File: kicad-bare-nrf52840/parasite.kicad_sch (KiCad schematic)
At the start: 29 parts, among them Q1 MMBT3906, Q4 Q_Photo_NPN, SW1 B3U-1000P, U1 E73-2G4M08S1C, U2 SHTC3, Y1 32.768kHz

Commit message: feat: capture bare nRF52840 circuit with verified Nordic support networks
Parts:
- removed RST1, SW1: B3U-1000P, SW_B3U-1000P, symbol B3U-1000P:B3U-1000P
- removed U1: E73-2G4M08S1C, snapeda:E73-2G4M08S1C, symbol E73:E73-2G4M08S1C
- added AE1: 2450AT18B0100001E, RF_Antenna:Johanson_2450AT18x100, symbol Device:Antenna_Chip
- added C10, C5, C8, C9: 100n, Capacitor_SMD:C_0402_1005Metric, symbol Device:C_Small
- added C11, C7: 1u, Capacitor_SMD:C_0402_1005Metric, symbol Device:C_Small
- added C12: 47n, Capacitor_SMD:C_0402_1005Metric, symbol Device:C_Small
- added C13: 100p, Capacitor_SMD:C_0402_1005Metric, symbol Device:C_Small
- added C14, C15: 12p, Capacitor_SMD:C_0402_1005Metric, symbol Device:C_Small
- added C16: 820p, Capacitor_SMD:C_0402_1005Metric, symbol Device:C_Small
- added C17: 0.8p, Capacitor_SMD:C_0402_1005Metric, symbol Device:C_Small
- added C18: 0.5p, Capacitor_SMD:C_0402_1005Metric, symbol Device:C_Small
- added C19: 1.2p, Capacitor_SMD:C_0402_1005Metric, symbol Device:C_Small
- added C6: 4.7u, Capacitor_SMD:C_0402_1005Metric, symbol Device:C_Small
- added L1: 10u, Inductor_SMD:L_0603_1608Metric, symbol Device:L
- added L2: 15n, Inductor_SMD:L_0402_1005Metric, symbol Device:L
- added L3: 4.7n, Inductor_SMD:L_0402_1005Metric, symbol Device:L
- added L4: 2.7n, Inductor_SMD:L_0402_1005Metric, symbol Device:L
- added L5: 3.3n, Inductor_SMD:L_0402_1005Metric, symbol Device:L
- added RST1, SW1: B3U-1000P, Button_Switch_SMD:SW_SPST_B3U-1000P, symbol Switch:SW_Push
- added U1: nRF52840-QIAA, Package_DFN_QFN:Nordic_AQFN-73-1EP_7x7mm_P0.5mm, symbol MCU_Nordic:nRF52840
- added Y2: 32MHz, Crystal:Crystal_SMD_2016-4Pin_2.0x1.6mm, symbol Device:Crystal_GND24
- D1: LCSC C3011166 -> C9808
- TP1: value IO -> SWDIO; now in the parts list
- TP2: value CLK -> SWDCLK; now in the parts list
- TP3, TP4, TP5, TP6, TP8: now in the parts list
- TP7: value VCC -> +3V0; now in the parts list
- Y1: MPN (none) -> NX3215SA-32.768K-STD-MUA-9; Source (none) -> PCA10056 3.0.3 BOM
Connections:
- net +3V0: now also C10.1, C6.1, C7.1, C8.1, C9.1, U1.A22 (VDD), U1.AD14 (VDD), U1.AD23 (VDD), U1.B1 (VDD), U1.W1 (VDD), U1.Y2 (VDDH)
- net 0.10: now also U1.J24 (NFC2/P0.10)
- net BTN1: now also SW1.1, U1.B9 (AIN6/P0.30)
- net GND: now also C10.2, C11.2, C12.2, C13.2, C14.2, C15.2, C16.2, C17.2, C18.2, C5.2, C6.2, C7.2, C8.2, C9.2, L4.2, RST1.2, SW1.2, U1.AD2 (VBUS), U1.B7 (VSS), U1.EP (VSS), U1.F23 (VSS_PA), Y2.2 (G), Y2.4 (G)
- net LED: now also U1.B11 (AIN4/P0.28)
- net PHOTO_OUT: now also U1.A12 (AIN0/P0.02)
- net PHOTO_V: now also U1.A10 (AIN5/P0.29)
- net PWM: now also U1.K2 (AIN3/P0.05)
- net RST: now also RST1.1, U1.AC13 (P0.18/~{RESET})
- net SCL: now also U1.AD8 (P0.13)
- net SDA: now also U1.AD20 (P0.24)
- net SENS_OUT: now also U1.B13 (AIN1/P0.03)
- net SWDCLK: now also U1.AA24 (SWDCLK)
- net SWDIO: now also U1.AC24 (SWDIO)
- net XL1: now reaches C3.2, Y1.2
- net XL1: now also U1.D2 (XL1/P0.00)
- net XL2: now reaches C4.1, Y1.1
- net XL2: now also U1.F2 (XL2/P0.01)
- new net: L1.2, L2.1
- new net ANT_FEED: AE1.1 (FEED), L5.2
- new net ANT_TUNE: C19.2, L4.1, L5.1
- new net DCC: L1.1, U1.B3 (DCC)
- new net DEC1: C5.1, U1.C1 (DEC1)
- new net DEC3: C13.1, U1.D23 (DEC3)
- new net DEC4_6: C11.1, C12.1, L2.2, U1.B5 (DEC4), U1.E24 (DEC6)
- new net DEC5: C16.1, U1.N24 (DEC5)
- new net RF_50: C18.1, C19.1, L3.2
- new net RF_SOC: C17.1, L3.1, U1.H23 (ANT)
- new net XC1: C14.1, U1.B24 (XC1), Y2.1
- new net XC2: C15.1, U1.A23 (XC2), Y2.3
- no-connect marks 25 -> 43
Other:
- note removed: "Battery clip"
- note removed: "Fast discharge on PWM’s low cycle"
- note removed: "LED"
- note removed: "Light sensor"
- note removed: "Parasitic capacitor sensing"
- note removed: "Reset switch"
- note removed: "Temperature and humidity sensor"
- note removed: "Test pads"
- note removed: "User button"
- note removed: "nRF52 module"
- title: b-parasite -> b-parasite — bare nRF52840

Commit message: feat: place bare MCU support circuitry and route critical analog networks
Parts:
- RST1, SW1: footprint Button_Switch_SMD:SW_SPST_B3U-1000P -> snapeda:SW_B3U-1000P

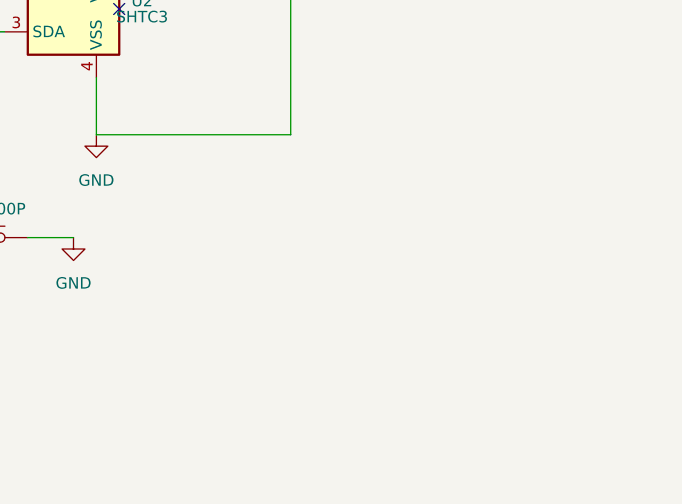
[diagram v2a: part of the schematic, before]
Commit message: feat: add Tag-Connect SWD port and free MCU fanout with compact battery contacts
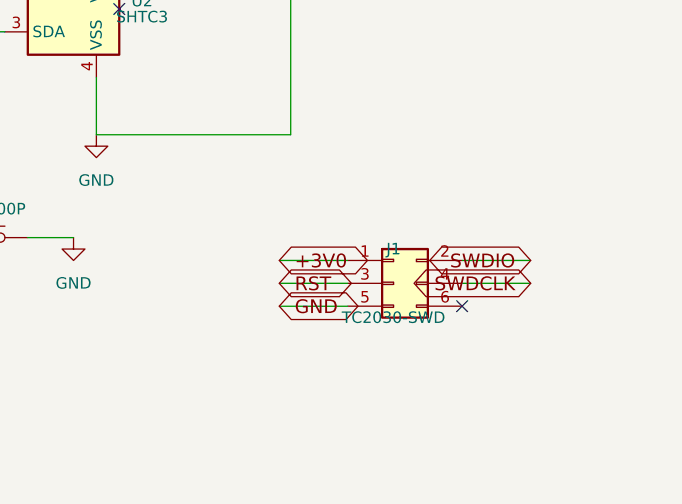
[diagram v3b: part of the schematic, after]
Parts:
- added J1: TC2030-SWD, Connector:Tag-Connect_TC2030-IDC-NL_2x03_P1.27mm_Vertical, symbol Connector_Generic:Conn_02x03_Odd_Even
- BT1: footprint kicad:BatteryHolder_Keystone_3002_1x2032 -> Battery:BatteryHolder_Keystone_1060_1x2032; MPN (none) -> 1060
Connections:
- net +3V0: now also J1.1 (Pin_1)
- net GND: now also J1.5 (Pin_5)
- net RST: now also J1.3 (Pin_3)
- net SWDCLK: now also J1.4 (Pin_4)
- net SWDIO: now also J1.2 (Pin_2)
- no-connect marks 43 -> 44
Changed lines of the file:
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@@
 			)
 		)
-		(property "Footprint" "kicad:BatteryHolder_Keystone_3002_1x2032"
+		(property "Footprint" "Battery:BatteryHolder_Keystone_1060_1x2032"
 			(at 180.34 240.03 0)
 			(hide yes)
@@
 		(pin "2"
 		)
+		(property "MPN" "1060"
+			(at 180.34 240.03 0)
+			(effects (font (size 1.27 1.27)) (hide yes))
+		)
 		(instances
 			(project "parasite"
@@
 		)
 	)
+	(symbol
+		(lib_id "Connector_Generic:Conn_02x03_Odd_Even")
+		(at 375.92 245.11 0)
+		(unit 1)
+		(exclude_from_sim no)
+		(in_bom yes)
+		(on_board yes)
+		(dnp no)
+		(property "Reference" "J1"
+			(at 375.92 241.3 0)
+			(effects (font (size 1.27 1.27)))
+		)
+		(property "Value" "TC2030-SWD"
+			(at 375.92 248.92 0)
+			(effects (font (size 1.27 1.27)))
+		)
+		(property "Footprint" "Connector:Tag-Connect_TC2030-IDC-NL_2x03_P1.27mm_Vertical"
+			(at 375.92 245.11 0)
+			(effects (font (size 1.27 1.27)) (hide yes))
+		)
+		(property "Datasheet" "~"
+			(at 375.92 245.11 0)
+			(effects (font (size 1.27 1.27)) (hide yes))
+		)
+		(instances
+			(project "parasite"
+				(path "/cfc3669b-133b-4df2-9732-7acc04e190be"
+					(reference "J1") (unit 1)
+				)
+			)
+		)
+	)
+	(global_label "+3V0"
+		(shape bidirectional)
+		(at 363.22 242.57 0)
+		(effects (font (size 1.524 1.524)) (justify left))
+	)
+	(global_label "SWDIO"
+		(shape bidirectional)
+		(at 391.16 242.57 180)
+		(effects (font (size 1.524 1.524)) (justify right))
+	)
+	(global_label "RST"
+		(shape bidirectional)
+		(at 363.22 245.11 0)
+		(effects (font (size 1.524 1.524)) (justify left))
+	)
+	(global_label "SWDCLK"
+		(shape bidirectional)
+		(at 391.16 245.11 180)
+		(effects (font (size 1.524 1.524)) (justify right))
+	)
+	(global_label "GND"
+		(shape bidirectional)
+		(at 363.22 247.65 0)
+		(effects (font (size 1.524 1.524)) (justify left))
+	)
+	(no_connect (at 383.54 247.65))
 	(wire
 		(pts (xy 26.67 139.7) (xy 31.75 139.7))
@@
 		(stroke (width 0) (type solid))
 	)
+	(wire
+		(pts (xy 363.22 242.57) (xy 370.84 242.57))
+		(stroke (width 0) (type solid))
+	)
+	(wire
+		(pts (xy 383.54 242.57) (xy 391.16 242.57))
+		(stroke (width 0) (type solid))
+	)
+	(wire
+		(pts (xy 363.22 245.11) (xy 370.84 245.11))
+		(stroke (width 0) (type solid))
+	)
+	(wire
+		(pts (xy 383.54 245.11) (xy 391.16 245.11))
+		(stroke (width 0) (type solid))
+	)
+	(wire
+		(pts (xy 363.22 247.65) (xy 370.84 247.65))
+		(stroke (width 0) (type solid))
+	)

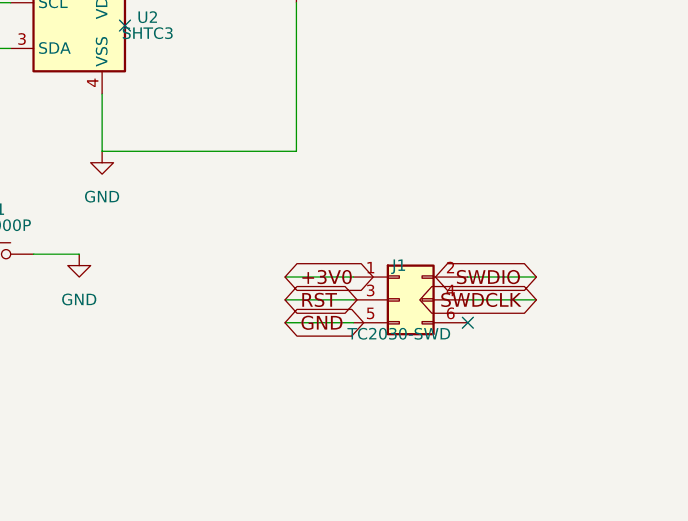
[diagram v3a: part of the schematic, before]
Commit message: checkpoint: before via-in-pad MCU fanout refinement
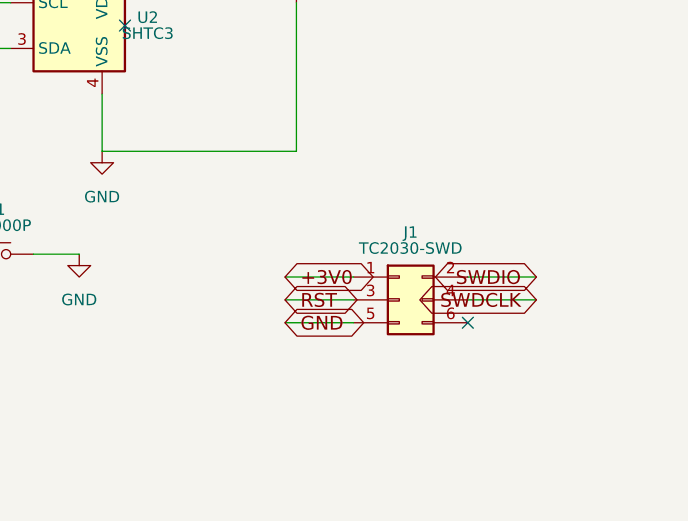
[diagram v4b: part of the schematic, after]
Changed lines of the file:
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@@
 		(dnp no)
 		(property "Reference" "J1"
-			(at 375.92 241.3 0)
+			(at 377.19 237.617 0)
 			(effects (font (size 1.27 1.27)))
 		)
 		(property "Value" "TC2030-SWD"
-			(at 375.92 248.92 0)
+			(at 377.19 239.395 0)
 			(effects (font (size 1.27 1.27)))
 		)

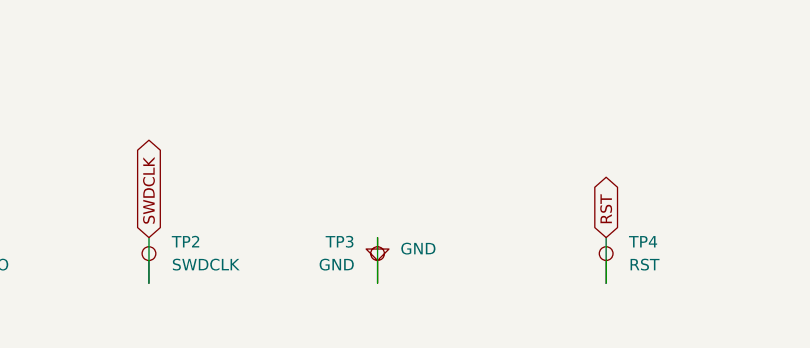
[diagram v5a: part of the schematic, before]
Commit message: feat: reconcile PCB library links and validate complete schematic parity
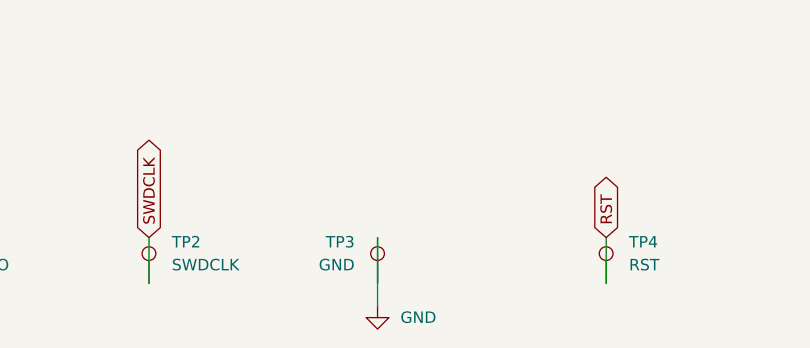
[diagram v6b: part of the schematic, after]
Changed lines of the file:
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@@
 	(symbol
 		(lib_id "power:GND")
-		(at 85.09 260.35 0)
+		(at 85.09 267.97 0)
 		(unit 1)
 		(body_style 1)
@@
 		(fields_autoplaced yes)
 		(property "Reference" "#PWR026"
-			(at 85.09 266.7 0)
+			(at 85.09 274.32 0)
 			(hide yes)
 			(show_name no)
@@
 		)
 		(property "Value" "GND"
-			(at 87.63 261.6199 0)
+			(at 87.63 269.2399 0)
 			(show_name no)
 			(do_not_autoplace no)
@@
 		)
 		(property "Footprint" ""
-			(at 85.09 260.35 0)
+			(at 85.09 267.97 0)
 			(hide yes)
 			(show_name no)
@@
 		)
 		(property "Datasheet" ""
-			(at 85.09 260.35 0)
+			(at 85.09 267.97 0)
 			(hide yes)
 			(show_name no)
@@
 		)
 		(property "Description" ""
-			(at 85.09 260.35 0)
+			(at 85.09 267.97 0)
 			(show_name no)
 			(do_not_autoplace no)
@@
 		(stroke (width 0) (type solid))
 	)
+	(wire
+		(pts (xy 85.09 260.35) (xy 85.09 267.97))
+		(stroke (width 0) (type solid))
+	)

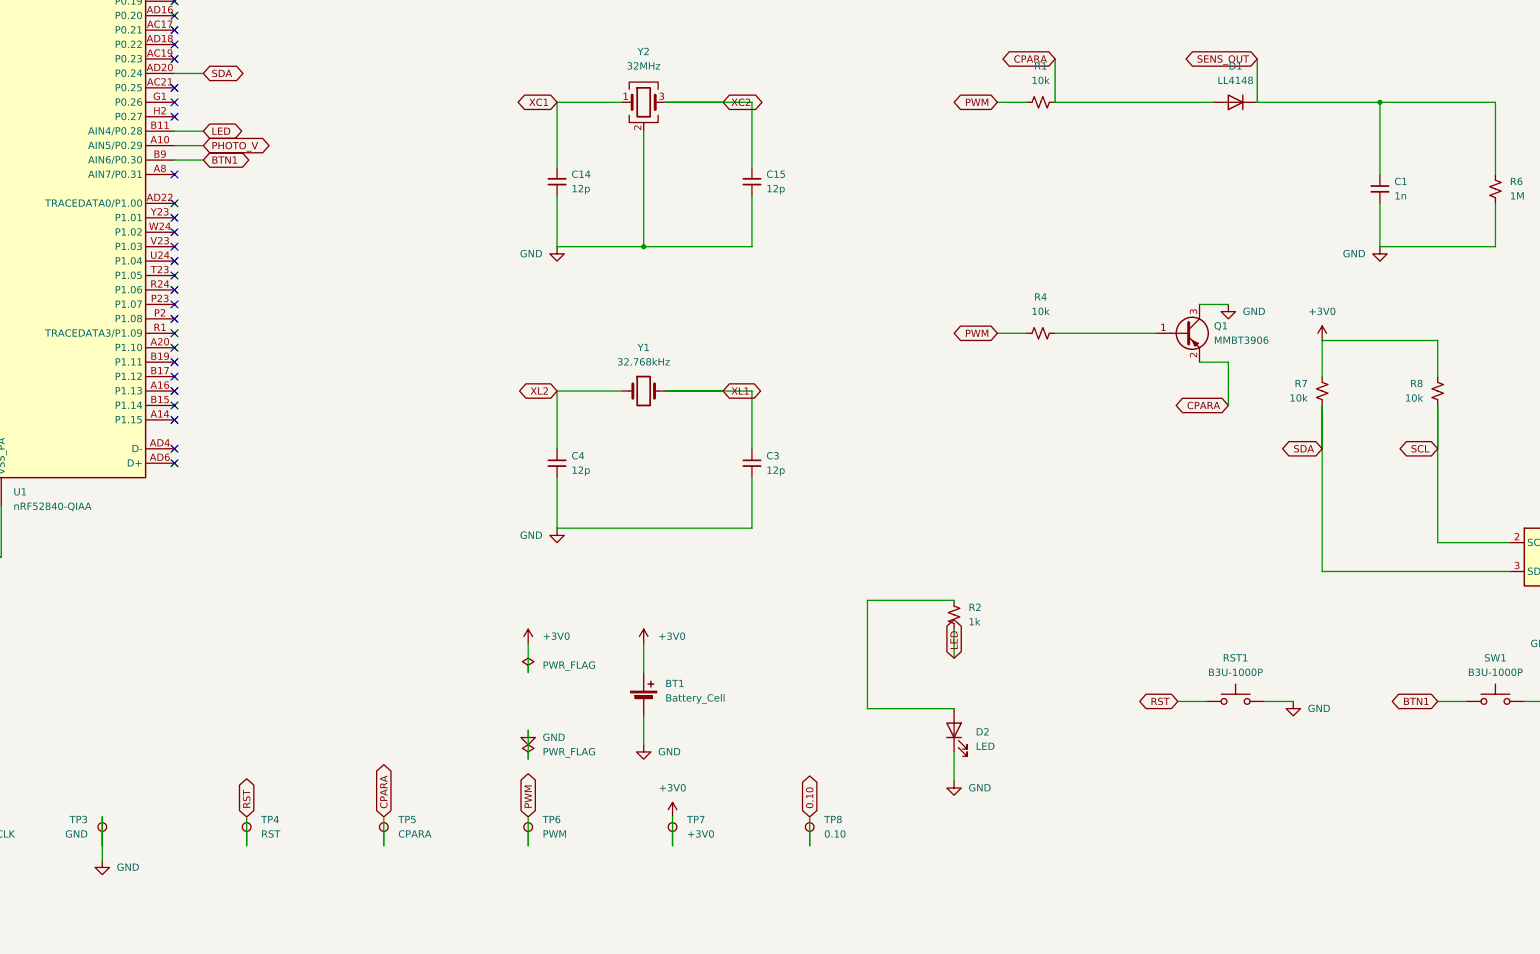
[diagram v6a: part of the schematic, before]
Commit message: feat: resolve KiCad warnings and align stackup and sourcing for fabrication
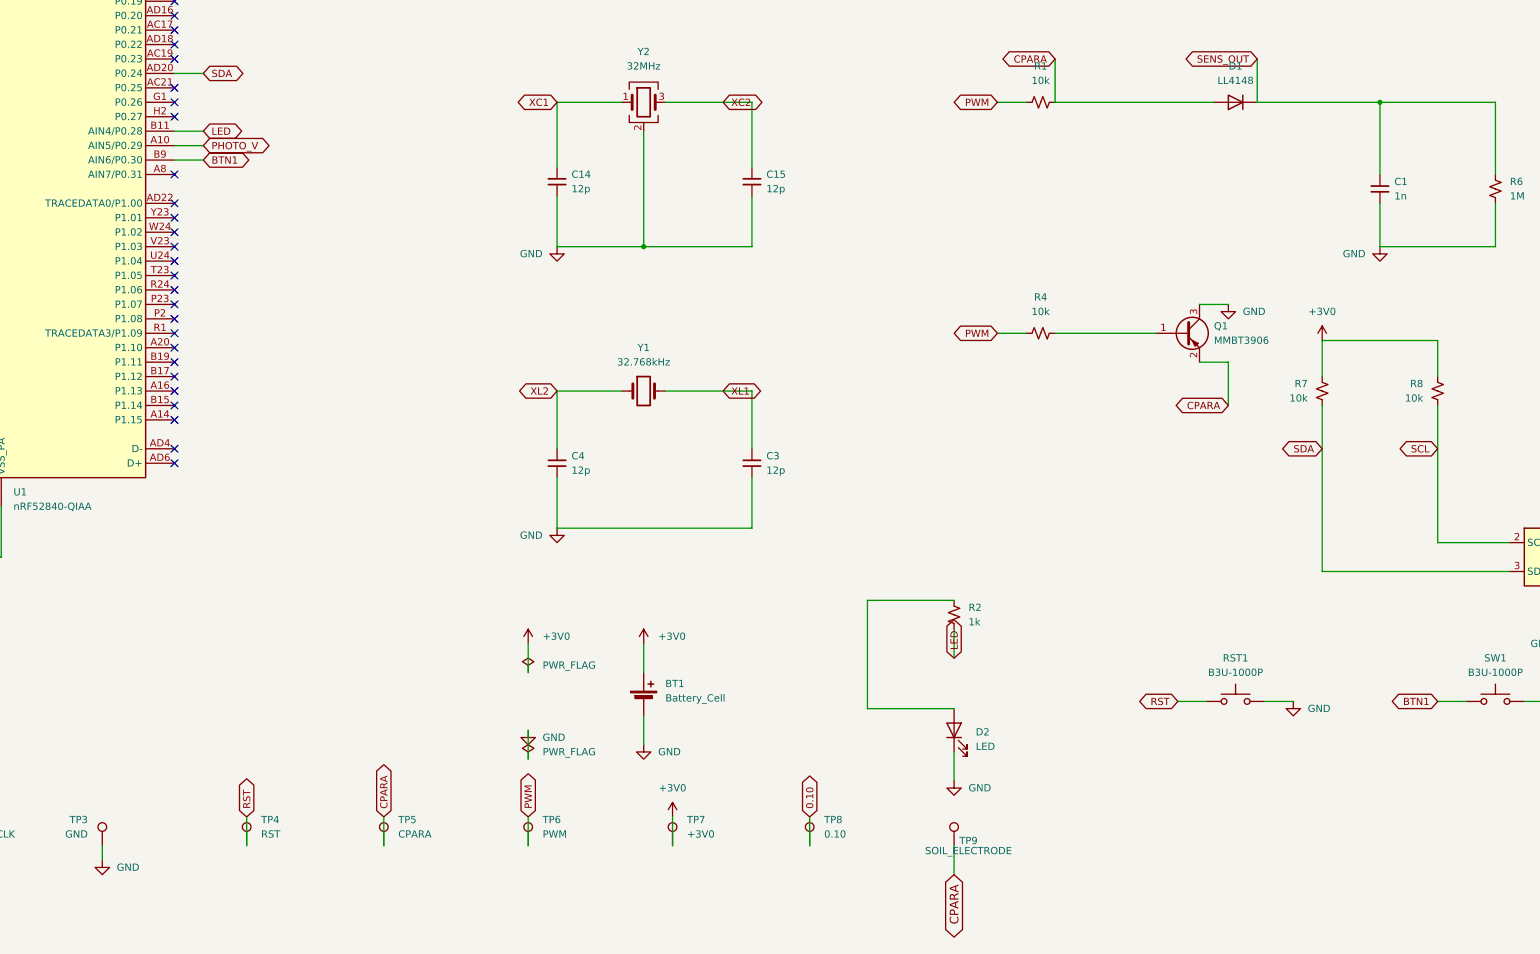
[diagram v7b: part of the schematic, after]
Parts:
- added TP9: SOIL_ELECTRODE, b-parasite:Soil_Electrode_Endpoint_Covered, symbol Connector:TestPoint
- BT1: footprint Battery:BatteryHolder_Keystone_1060_1x2032 -> b-parasite:BatteryHolder_Keystone_1060_NoBodySilk
- Q4: MPN (none) -> ALS-PT19-315C/L177/TR8
- U1: LCSC (none) -> C190794; MPN nRF52840-QIAA -> NRF52840-QIAA-R
- Y1: Assembly_note (none) -> NDK NX3215SA-32.768K-STD-MUA-9; 9 pF load. Do not substitut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; LCSC C32346 -> (none)
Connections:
- net CPARA: now also TP9.1

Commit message: feat: specify JLCPCB sourcing and ENIG construction for the reviewed prototype
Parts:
- AE1: LCSC (none) -> C6055600; Manufacturer Johanson Technology -> Johanson
- BT1: LCSC (none) -> C5370859; Manufacturer (none) -> Keystone
- C1: MPN (none) -> 0402B102K500NT; Manufacturer (none) -> FH
- C10, C5, C8, C9: LCSC (none) -> C1525; MPN (none) -> CL05B104KO5NNNC; Manufacturer (none) -> Samsung
- C11, C7: LCSC (none) -> C52923; MPN (none) -> CL05A105KA5NQNC; Manufacturer (none) -> Samsung
- C12: LCSC (none) -> C318631; MPN (none) -> CL05B473KA5NNNC; Manufacturer (none) -> Samsung
- C13: LCSC (none) -> C26409; MPN (none) -> CL05C101JB5NNNC; Manufacturer (none) -> Samsung
- C14, C15: LCSC (none) -> C1547; MPN (none) -> 0402CG120J500NT; Manufacturer (none) -> FH
- C16: Assembly_note Optional for Fxx and later; fit for earlier builds -> Populate in this prototype variant, including Fxx and later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; LCSC (none) -> C307452; MPN (none) -> CL05C821JB5NNNC; Manufacturer (none) -> Samsung
- C17: LCSC (none) -> C76988; MPN (none) -> GRM1555C1HR80BA01D; Manufacturer (none) -> Murata
- C18: LCSC (none) -> C88941; MPN (none) -> GRM1555C1HR50WA01D; Manufacturer (none) -> Murata
- C19: LCSC (none) -> C76954; MPN (none) -> GRM1555C1H1R2BA01D; Manufacturer (none) -> Murata
- C2: MPN (none) -> CL05B104KO5NNNC; Manufacturer (none) -> Samsung
- C3, C4: MPN (none) -> 0402CG120J500NT; Manufacturer (none) -> FH
- C6: LCSC (none) -> C23733; MPN (none) -> CL05A475MP5NRNC; Manufacturer (none) -> Samsung
- D1: MPN (none) -> LL4148; Manufacturer (none) -> Semtech
- D2: MPN (none) -> KT-0603R; Manufacturer (none) -> Hubei KENTO
- L1: LCSC (none) -> C2047264; Manufacturer (none) -> TDK
- L2: LCSC (none) -> C86059; Manufacturer (none) -> Murata
- L3: LCSC (none) -> C162543; Manufacturer (none) -> Murata
- L4: LCSC (none) -> C77108; MPN (none) -> LQG15HS2N7S02D; Manufacturer (none) -> Murata
- L5: LCSC (none) -> C86064; MPN (none) -> LQG15HS3N3S02D; Manufacturer (none) -> Murata
- Q1: MPN (none) -> MMBT3906; Manufacturer (none) -> JSCJ
- R1, R4, R7, R8: MPN (none) -> 0402WGF1002TCE; Manufacturer (none) -> UNI-ROYAL
- R10: MPN (none) -> 0402WGF4700TCE; Manufacturer (none) -> UNI-ROYAL
- R2: MPN (none) -> 0402WGF1001TCE; Manufacturer (none) -> UNI-ROYAL
- R6: MPN (none) -> 0402WGF1004TCE; Manufacturer (none) -> UNI-ROYAL
- RST1, SW1: MPN (none) -> B3U-1000P; Manufacturer (none) -> Omron
- U2: MPN (none) -> SHTC3; Manufacturer (none) -> Sensirion
- Y1: Assembly_note NDK NX3215SA-32.768K-STD-MUA-9; 9 pF load. Do not substitut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 -> 9 pF load; C519280 matches exact NDK MPN. Do not substitute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; LCSC (none) -> C519280; Manufacturer (none) -> NDK
- Y2: Assembly_note (none) -> Golledge custom MP12308 from Nordic reference; 32 MHz, CL 8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
